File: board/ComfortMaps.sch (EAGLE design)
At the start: 50 parts, among them J1 PROG_HDR, U1 ADXL362, U3 ADP160-3.3, U4 MCP73833, X1 RASPI_GPIO_B+#_PIN

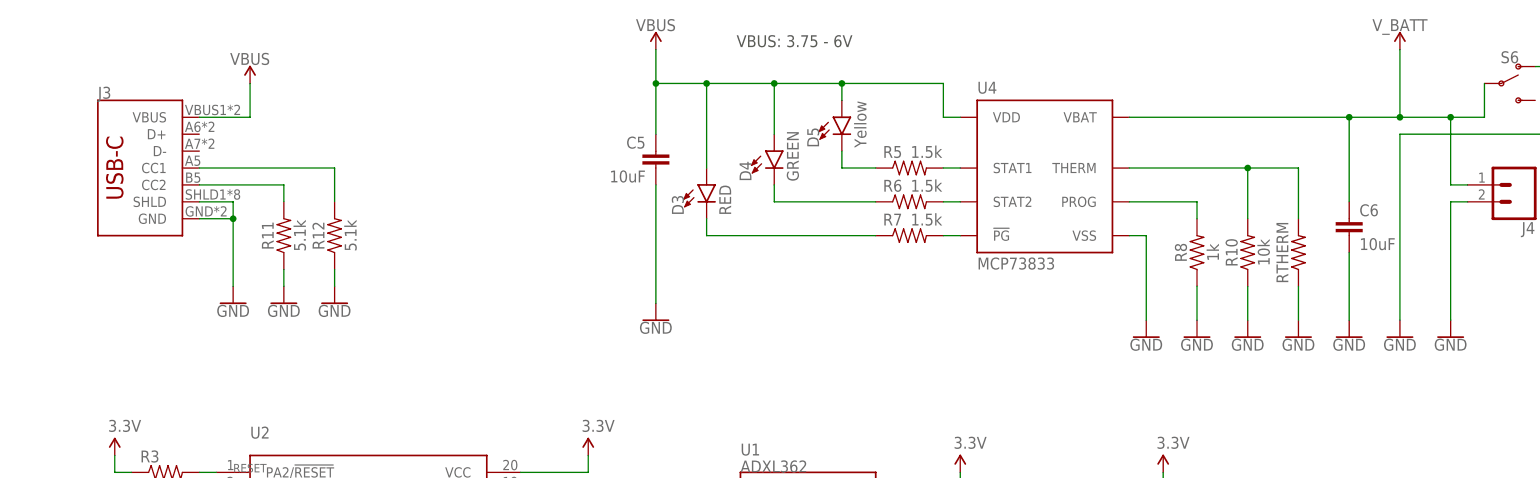
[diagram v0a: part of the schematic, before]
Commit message: V5 board, with new usb type c connector and lipo charge controller.
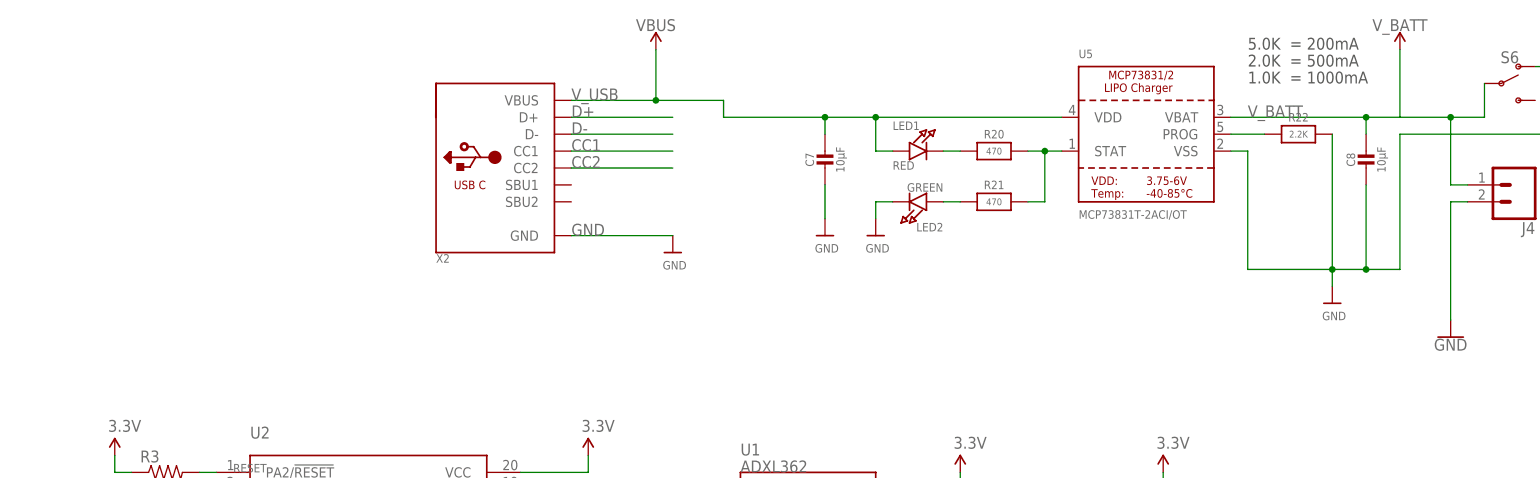
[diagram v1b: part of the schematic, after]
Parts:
- removed C5, C6: 10uF, SparkFun-Capacitors:10UF-0603-6.3V-20%
- removed D3: RED, SparkFun-LED:LED-RED0603
- removed D4: GREEN, SparkFun-LED:LED-GREEN0603
- removed D5: Yellow, SparkFun-LED:LED-YELLOW0603
- removed J3: (no value), SparkFun-Connectors:USB_C16PIN
- removed R10: 10k, SparkFun-Resistors:10KOHM-0603-1/10W-1%
- removed R11, R12: 5.1k, SparkFun-Resistors:5.1KOHM5.1KOHM-0603-1/10W-1%
- removed R5, R6, R7: 1.5k, SparkFun-Resistors:1.5KOHM-0603-1/10W-1%
- removed R8: 1k, SparkFun-Resistors:1KOHM-0603-1/10W-1%
- removed RTHERM: THERM, resistor:R-US_R0805
- removed U4: MCP73833, SparkFun-IC-Power:MCP73833
- added C7, C8: 10µF, microbuilder:CAP_CERAMIC0805-NOOUTLINE
- added LED1: RED, microbuilder:LED0805_NOOUTLINE
- added LED2: GREEN, microbuilder:LED0805_NOOUTLINE
- added R20, R21: 470, microbuilder:RESISTOR_0603_NOOUT
- added R22: 2.2K, microbuilder:RESISTOR_0603_NOOUT
- added U5: MCP73831T-2ACI/OT, microbuilder:MCP73831/2
- added X2: (no value), microbuilder:USB_C
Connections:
- removed net N$10: D4.C, R6.1
- removed net N$11: D5.C, R5.1
- removed net N$12: J3.CC2, R11.2
- removed net N$13: J3.CC1, R12.2
- removed net N$9: D3.C, R7.1
- removed net PG: R7.2, U4.!PG
- removed net PROG: R8.2, U4.PROG
- removed net STAT1: R5.2, U4.STAT1
- removed net STAT2: R6.2, U4.STAT2
- removed net THERM: R10.2, RTHERM.2, U4.THERM
- new net CC1: X2.CC1
- new net CC2: X2.CC2
- new net D+: X2.D+
- new net D-: X2.D-
- new net N$17: LED1.C, R20.1
- new net N$18: R20.2, R21.2, U5.STAT
- new net N$19: R22.1, U5.PROG
- new net N$20: LED2.A, R21.1
- net GND: now also C7.2, C8.2, LED2.C, R22.2, U5.VSS, X2.GND; no longer C5.2, C6.2, J3.GND, J3.SHLD, R10.1, R11.1, R12.1, R8.1, RTHERM.1, U4.VSS
- net V_BATT: now also C8.1, U5.VBAT; no longer C6.1, U4.VBAT
- net V_USB: now also C7.1, LED1.A, U5.VDD, X2.VBUS; no longer C5.1, D3.A, D4.A, D5.A, J3.VBUS, U4.VDD
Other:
- note added: "1.0K = 1000mA"
- note added: "2.0K = 500mA"
- note added: "5.0K = 200mA"
- note removed: "VBUS: 3.75 - 6V"

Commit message: V5
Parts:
- S6: value (none) -> MA12RTR; DIGIKEY (none) -> 679-1847-1-ND
- U2: value (none) -> ATTINY2313
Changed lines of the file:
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@@
 <?xml version="1.0" encoding="utf-8"?>
 <!DOCTYPE eagle SYSTEM "eagle.dtd">
-<eagle version="9.5.1">
+<eagle version="9.5.2">
 <drawing>
 <settings>
@@
 <part name="J1" library="SparkFun-Connectors" deviceset="AVR_SPI_PRG_6" device="PTH" value="PROG_HDR"/>
 <part name="GND1" library="SparkFun-Aesthetics" deviceset="GND" device=""/>
-<part name="U2" library="SparkFun-DigitalIC" deviceset="ATTINY2313A" device="">
+<part name="U2" library="SparkFun-DigitalIC" deviceset="ATTINY2313A" device="" value="ATTINY2313">
 <attribute name="DIST" value="DIGIKEY"/>
 <attribute name="DIST_ID" value="ATTINY2313A-SU-ND"/>
@@
 <part name="D1" library="SparkFun-LED" deviceset="LED-RED" device="0603" value="RED"/>
 <part name="R17" library="SparkFun-Resistors" deviceset="1.5KOHM" device="-0603-1/10W-1%" value="1.5k"/>
-<part name="S6" library="SparkFun-Switches" library_urn="urn:adsk.eagle:library:535" deviceset="SWITCH-SPDT" device="-SMD-RIGHT-ANGLE" package3d_urn="urn:adsk.eagle:package:40179/1"/>
+<part name="S6" library="SparkFun-Switches" library_urn="urn:adsk.eagle:library:535" deviceset="SWITCH-SPDT" device="-SMD-RIGHT-ANGLE" package3d_urn="urn:adsk.eagle:package:40179/1" value="MA12RTR">
+<attribute name="DIGIKEY" value="679-1847-1-ND"/>
+</part>
 <part name="R18" library="SparkFun-Resistors" deviceset="10K-1%" device="RES-00824" value="10k"/>
 <part name="D2" library="SparkFun-LED" deviceset="LED-RED" device="0603" value="RED"/>
@@
 <attribute name="NAME" x="227.33" y="196.088" size="1.778" layer="95" font="vector" align="bottom-center"/>
 <attribute name="VALUE" x="227.076" y="189.738" size="1.778" layer="96" font="vector" align="top-center"/>
+<attribute name="DIGIKEY" x="226.06" y="193.04" size="1.778" layer="96" display="off"/>
 </instance>
 <instance part="R18" gate="G$1" x="284.48" y="55.88" smashed="yes" rot="R270">

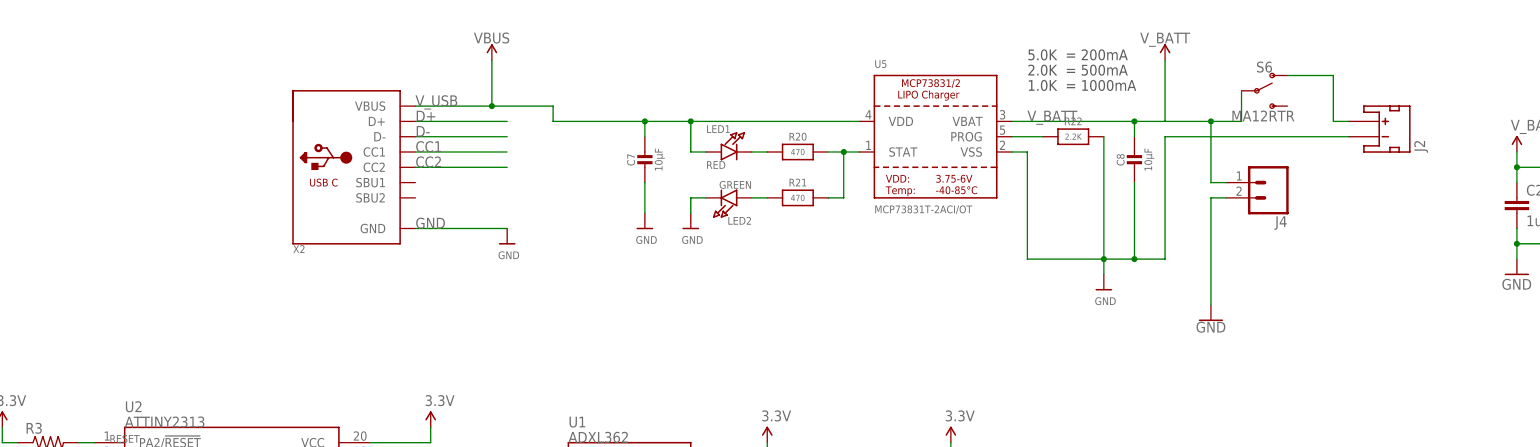
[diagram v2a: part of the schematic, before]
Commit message: Moving back to older lipo charger.
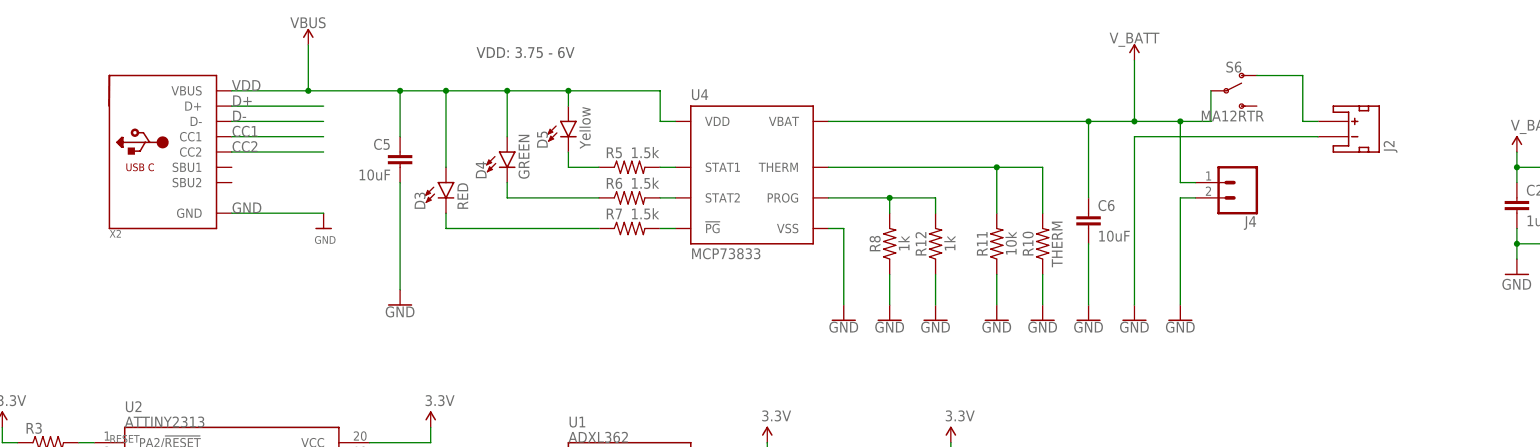
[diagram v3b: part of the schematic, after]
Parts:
- removed C7, C8: 10µF, microbuilder:CAP_CERAMIC0805-NOOUTLINE
- removed LED1: RED, microbuilder:LED0805_NOOUTLINE
- removed LED2: GREEN, microbuilder:LED0805_NOOUTLINE
- removed R20, R21: 470, microbuilder:RESISTOR_0603_NOOUT
- removed R22: 2.2K, microbuilder:RESISTOR_0603_NOOUT
- removed U5: MCP73831T-2ACI/OT, microbuilder:MCP73831/2
- added C5, C6: 10uF, SparkFun-Capacitors:10UF-0603-6.3V-20%
- added D3: RED, SparkFun-LED:LED-RED0603
- added D4: GREEN, SparkFun-LED:LED-GREEN0603
- added D5: Yellow, SparkFun-LED:LED-YELLOW0603
- added R10: THERM, SparkFun-Resistors:RESISTORAXIAL-0.3
- added R11: 10k, SparkFun-Resistors:10KOHM-0603-1/10W-1%
- added R12: 1k, SparkFun-Resistors:RESISTORAXIAL-0.3
- added R5, R6, R7: 1.5k, SparkFun-Resistors:1.5KOHM-0603-1/10W-1%
- added R8: 1k, SparkFun-Resistors:1KOHM-0603-1/10W-1%
- added U4: MCP73833, SparkFun-IC-Power:MCP73833
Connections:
- removed net N$17: LED1.C, R20.1
- removed net N$18: R20.2, R21.2, U5.STAT
- removed net N$19: R22.1, U5.PROG
- removed net N$20: LED2.A, R21.1
- removed net V_USB: C7.1, LED1.A, U5.VDD, X2.VBUS
- new net N$11: D4.C, R6.1
- new net N$12: D5.C, R5.1
- new net N$9: D3.C, R7.1
- new net PG: R7.2, U4.!PG
- new net PROG: R12.2, R8.2, U4.PROG
- new net STAT1: R5.2, U4.STAT1
- new net STAT2: R6.2, U4.STAT2
- new net THERM: R10.2, R11.2, U4.THERM
- new net VDD: C5.1, D3.A, D4.A, D5.A, U4.VDD, X2.VBUS
- net GND: now also C5.2, C6.2, R10.1, R11.1, R12.1, R8.1, U4.VSS; no longer C7.2, C8.2, LED2.C, R22.2, U5.VSS
- net V_BATT: now also C6.1, U4.VBAT; no longer C8.1, U5.VBAT
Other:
- note added: "VDD: 3.75 - 6V"
- note removed: "1.0K = 1000mA"
- note removed: "2.0K = 500mA"
- note removed: "5.0K = 200mA"
- moved on the sheet: J2, J4, S6, X2

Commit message: v6 board
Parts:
- removed C6: 10uF, SparkFun-Capacitors:10UF-0603-6.3V-20%
- removed D3: RED, SparkFun-LED:LED-RED0603
- removed D4: GREEN, SparkFun-LED:LED-GREEN0603
- removed D5: Yellow, SparkFun-LED:LED-YELLOW0603
- removed J2: (no value), SparkFun-Connectors:JST_2MM_MALE
- removed J4: (no value), SparkFun-Connectors:CONN_021X02_NO_SILK
- removed R10: THERM, SparkFun-Resistors:RESISTORAXIAL-0.3
- removed R11: 10k, SparkFun-Resistors:10KOHM-0603-1/10W-1%
- removed R12: 1k, SparkFun-Resistors:RESISTORAXIAL-0.3
- removed R4: 10k, SparkFun-Resistors:10K-1%RES-00824
- removed R5, R6, R7: 1.5k, SparkFun-Resistors:1.5KOHM-0603-1/10W-1%
- removed R8: 1k, SparkFun-Resistors:1KOHM-0603-1/10W-1%
- removed S6: MA12RTR, SparkFun-Switches:SWITCH-SPDT-SMD-RIGHT-ANGLE
- removed U4: MCP73833, SparkFun-IC-Power:MCP73833
- added C10, C9: 4.7uF, SparkFun-Capacitors:4.7UF0603
- added C11, C7, C8: 22uF, SparkFun-Capacitors:22UF-0805-6.3V-20%
- added D10, D9: 3A/40V/500mV, SparkFun-DiscreteSemi:DIODE-SCHOTTKY-B340A
- added D11: RED, SparkFun-LED:LED-RED0603
- added D8: BLUE, SparkFun-LED:LED-BLUE0603
- added J5: PTH, SparkFun-Connectors:CONN_02
- added J6: JST, SparkFun-Connectors:CONN_02-JST-2MM-SMT
- added L1: 2.2UH3A, SparkFun-Coils:INDUCTOR-IFSC1515AHER2R2M01
- added R20: 1k, SparkFun-Resistors:1KOHM-0603-1/10W-1%
- added R21, R25: 750K, SparkFun-Resistors:750KOHM-0603-1/10W-1%
- added R22: 100k, SparkFun-Resistors:100KOHM-0603-1/10W-1%
- added R24: 4.7k, SparkFun-Resistors:4.7KOHM-0603-1/10W-1%
- added RPROG: 2.0k, SparkFun-Resistors:2.0KOHM-0603-1/10W-5%
- added S7: MA12RTR, SparkFun-Switches:SWITCH-SPDT-SMD-RIGHT-ANGLE
- added U5: MCP73831, SparkFun-IC-Power:MCP73831
- added U6: PAM2401, SparkFun-IC-Power:PAM2401
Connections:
- removed net N$11: D4.C, R6.1
- removed net N$12: D5.C, R5.1
- removed net N$15: J2.+, S6.O
- removed net PG: R7.2, U4.!PG
- removed net PROG: R12.2, R8.2, U4.PROG
- removed net STAT1: R5.2, U4.STAT1
- removed net STAT2: R6.2, U4.STAT2
- removed net THERM: R10.2, R11.2, U4.THERM
- removed net TX0: X1.RXD
- removed net VDD: C5.1, D3.A, D4.A, D5.A, U4.VDD, X2.VBUS
- removed net V_BATT: C2.1, C6.1, J4.1, Q1PMOS.S, R1.1, S6.P, U3.EN, U3.VIN, U4.VBAT
- new net 5V: C7.1, C8.1, D10.C, D11.A, D9.C, R13.2, R14.2, R15.2, R16.2, R21.2, R9.2, U6.OUT, X1.5V0A, X1.5V0B
- new net 5VIN: C5.1, C9.1, R20.2, U5.VIN, X2.VBUS
- new net EN: R25.1, U6.EN
- new net N$10: RPROG.1, U5.PROG
- new net N$13: D8.C, U5.STAT
- new net N$17: R21.1, R22.2, U6.FB
- new net N$18: L1.2, U6.LX
- new net N$19: U6.RSET
- new net N$21: D11.C, R24.2
- new net N$22: D8.A, R20.1
- new net VBATT: C10.1, C11.1, C2.1, L1.1, Q1PMOS.S, R1.1, R25.2, S7.P, U3.EN, U3.VIN, U5.VBAT, U6.VIN
- net 3.3V: no longer R13.2, R14.2, R15.2, R16.2, R4.1, R9.2
- net GND: now also C10.2, C11.2, C7.2, C8.2, C9.2, D10.A, D9.A, J5.2, J6.2, R22.1, R24.1, RPROG.2, U5.VSS, U6.AGND, U6.PGND; no longer C6.2, J2.-, J4.2, R10.1, R11.1, R12.1, R8.1, U4.VSS
- net N$9: now also J5.1, J6.1, S7.O; no longer D3.C, R7.1
- net RXI: no longer R4.2, X1.TXD
- net VOUT: no longer X1.5V0A, X1.5V0B
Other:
- note added: "2.0K resistor placed for 500mA charge rate"
- note added: "Battery connection"
- note added: "Charge power"
- note added: "Charger"
- note added: "Enable"
- note added: "Enable pin: To disable output, short EN pin to ground (is pulled up with 10kOhm)"
- note added: "For heavy duty use: Use 2A switch in switch bypass pins, or jump with wire."
- note added: "Install 100k resistor for inductor current limit"
- note added: "Ireg = 1000V/Rprog"
- note added: "LiPo Charger Booster"
- note added: "Marshall Taylor"
- note added: "Output capacity: 5V, 1A for 3.0V to 4.2V battery voltage."
- note added: "Switching Regulator"
- note added: "To charge battery, Minimize output load (or disable) Supply 3.75 to 6V, 500mA capable to USB or input voltage pins."
- note added: "v10"
